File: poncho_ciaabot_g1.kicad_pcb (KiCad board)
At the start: 2 copper layers, 86.5 x 137.5 mm, 26 parts, among them IC1 LM2577HV-ADJ, J1 CONN_01X02, J2 MOT_A, J3 MOT_B, J4 CONN_02X04, J5 CONN_01X03, J6 CONN_01X03, J7 CONN_01X03, J8 CONN_01X02, U1 POLOLU_A4988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

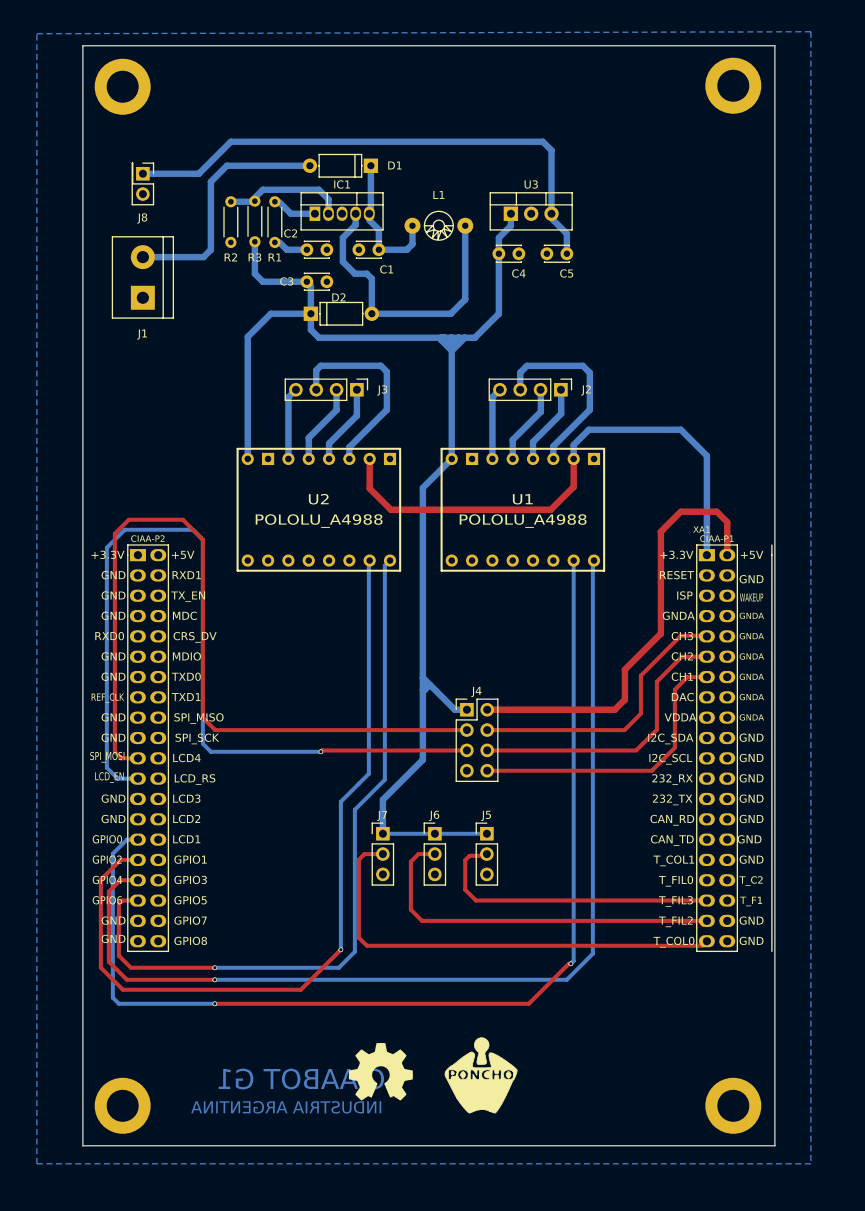
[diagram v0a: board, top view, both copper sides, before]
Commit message: Se agrega area de cobre en capa superior
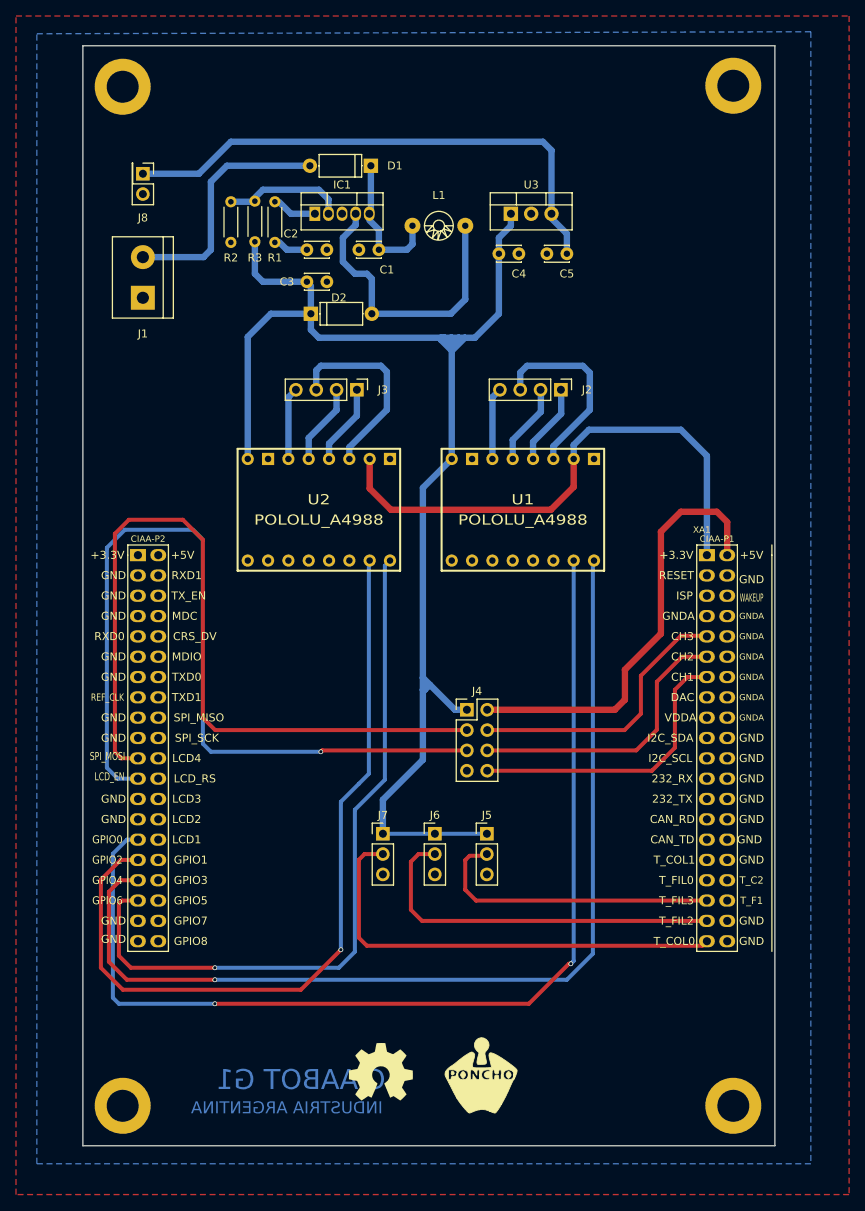
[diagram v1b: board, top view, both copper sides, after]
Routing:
- added copper zone on F.Cu, net (none)
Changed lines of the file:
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@@
     (links 75)
     (no_connects 0)
-    (area 112.424999 21.424999 199.075001 159.075001)
+    (area 106.75 19.75 203.500001 161.250001)
     (thickness 1.6)
     (drawings 6)
@@
       )
     )
+  )
+  (zone (net 0) (net_name "") (layer F.Cu) (hatch edge 0.508)
+    (connect_pads (clearance 0.508))
+    (min_thickness 0.254)
+    (fill yes (arc_segments 16) (thermal_gap 0.508) (thermal_bridge_width 0.508))
+    (polygon
+      (pts
+        (xy 208.28 165.1) (xy 104.14 165.1) (xy 104.14 17.78) (xy 208.28 17.78) (xy 208.28 165.1)
+      )
+    )
